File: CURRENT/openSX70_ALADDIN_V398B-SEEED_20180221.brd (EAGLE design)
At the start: 95.9 x 27.9 mm, 46 parts, among them Q1 5.8A/30V/35mΩ, Q2 5.8A/30V/35mΩ, U1 ATMEGA328P_TQFP, U3 BH1750FVI-TR, X1 FH12-10S-0.5SH, Y1 CSTCE8M00G52Z-R0

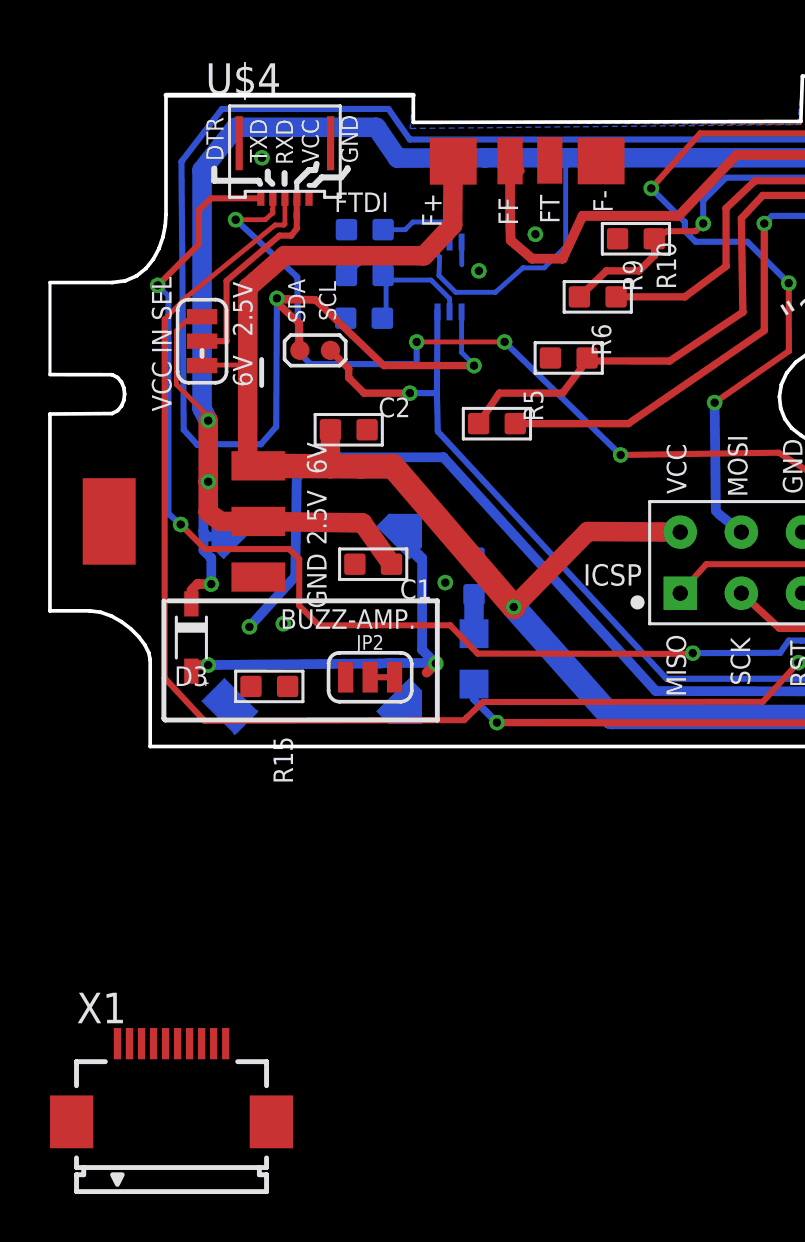
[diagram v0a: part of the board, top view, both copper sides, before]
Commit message: Latest with new Buzzer schematic
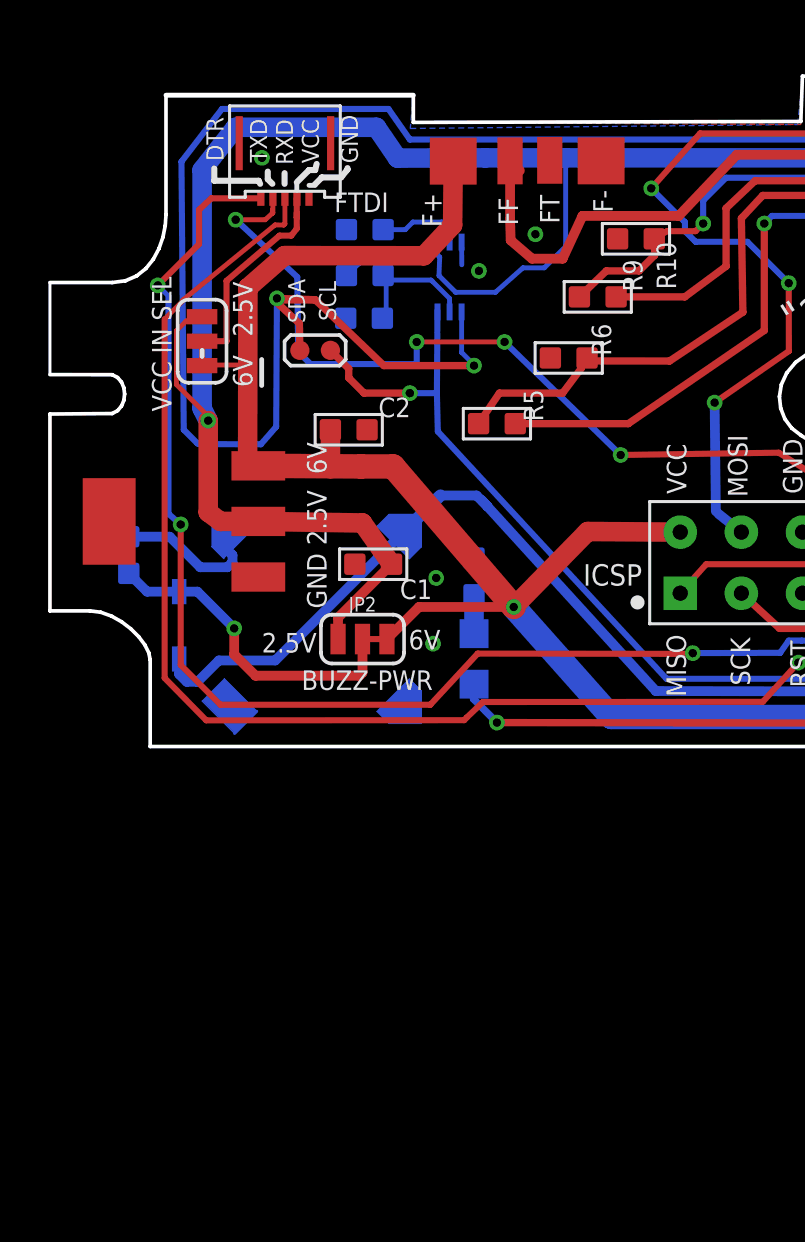
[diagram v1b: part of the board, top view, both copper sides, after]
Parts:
- removed X1: FH12-10S-0.5SH, con-hirose:FH12-10S-0.5SH
- moved R15 8.00 mm to (5.33, 8.76), flipped to the bottom, turned to 0 degrees
- moved JP2 1.62 mm to (15.0, 5.27)
- moved D3 0.72 mm to (7.43, 5.84), flipped to the bottom
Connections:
- removed net N$27: JP1.2, U$4.4
- net 3.3V: no longer D3.C, JP2.2, R15.2
- net 6V: now also D3.C, JP1.2, JP2.2, R15.2, U$4.4
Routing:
- net 6V: track 181.3 -> 209.4 mm, vias 5 -> 6
- net BUZZER: track 102.8 -> 87.4 mm, vias 6 -> 3
- net N$27: track 8.73 -> 0.00 mm
- net N$9: track 0.00 -> 6.43 mm
- net DTR: track 90.7 -> 94.8 mm
- net 3.3V: track 159.1 -> 157.3 mm, vias 9 -> 7
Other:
- board text added: "BUZZ-PWR"
- board text removed: "BUZZ-AMP."

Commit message: Clean-up board and schematic
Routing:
- net GND: track 27.9 -> 17.2 mm
- net FF: track 71.8 -> 70.7 mm
- net 3.3V: track 157.3 -> 156.3 mm
- net 100R: track 110.2 -> 109.2 mm
- net SOL1-: track 6.56 -> 7.47 mm
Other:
- board text added: "20180221"
- board text added: "layout 3.9.8BS"
- board text added: "openSX70 project visit www.openSX70.com version 3.9.8BS "Aladdin-fpc-S" 20170221 by Joaquín de Prada"
- board text removed: "20180219"
- board text removed: "layout 3.9.8S"
- board text removed: "layout 3.9.9S"
- board text removed: "openSX70 project visit www.openSX70.com version 3.9.8S "Aladdin-fpc-S" 20170219 by Joaquín de Prada"

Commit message: Tweaking and tweaking to keep the mind busy.
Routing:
- net GND: track 17.2 -> 15.5 mm, vias 15 -> 11
- net S3: track 15.2 -> 14.1 mm
- net S8@3.3V: track 70.3 -> 69.6 mm
- net S5: track 17.2 -> 16.5 mm
- net S2: track 20.1 -> 20.7 mm
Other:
- board text added: "ICSP"

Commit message: And so on...
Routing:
- net 6V: track 209.4 -> 205.4 mm
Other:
- board text added: "B-"
